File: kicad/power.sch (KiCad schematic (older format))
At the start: 30 parts, among them CON23 PS-ON, CON24 CON6, CON25 FAN, CON26 CON5x2, Q7 FDC6401N, Q8 FDC6401N, Q9 FDC6401N

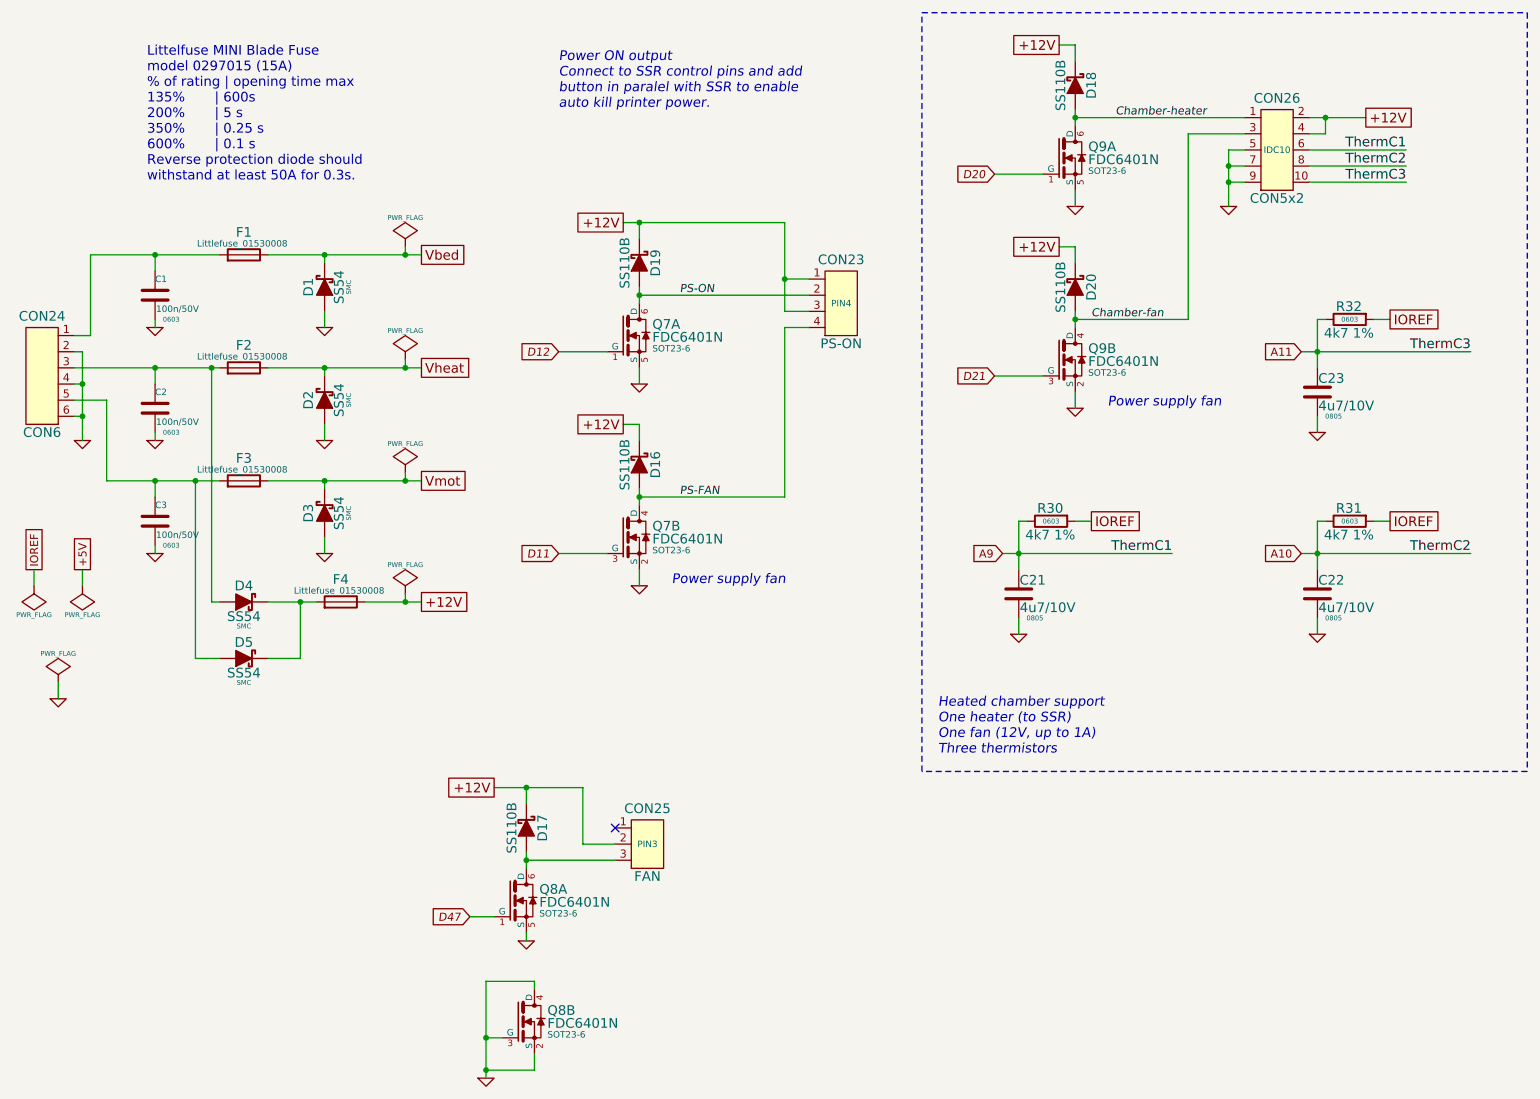
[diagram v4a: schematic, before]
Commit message: Add footprint informations
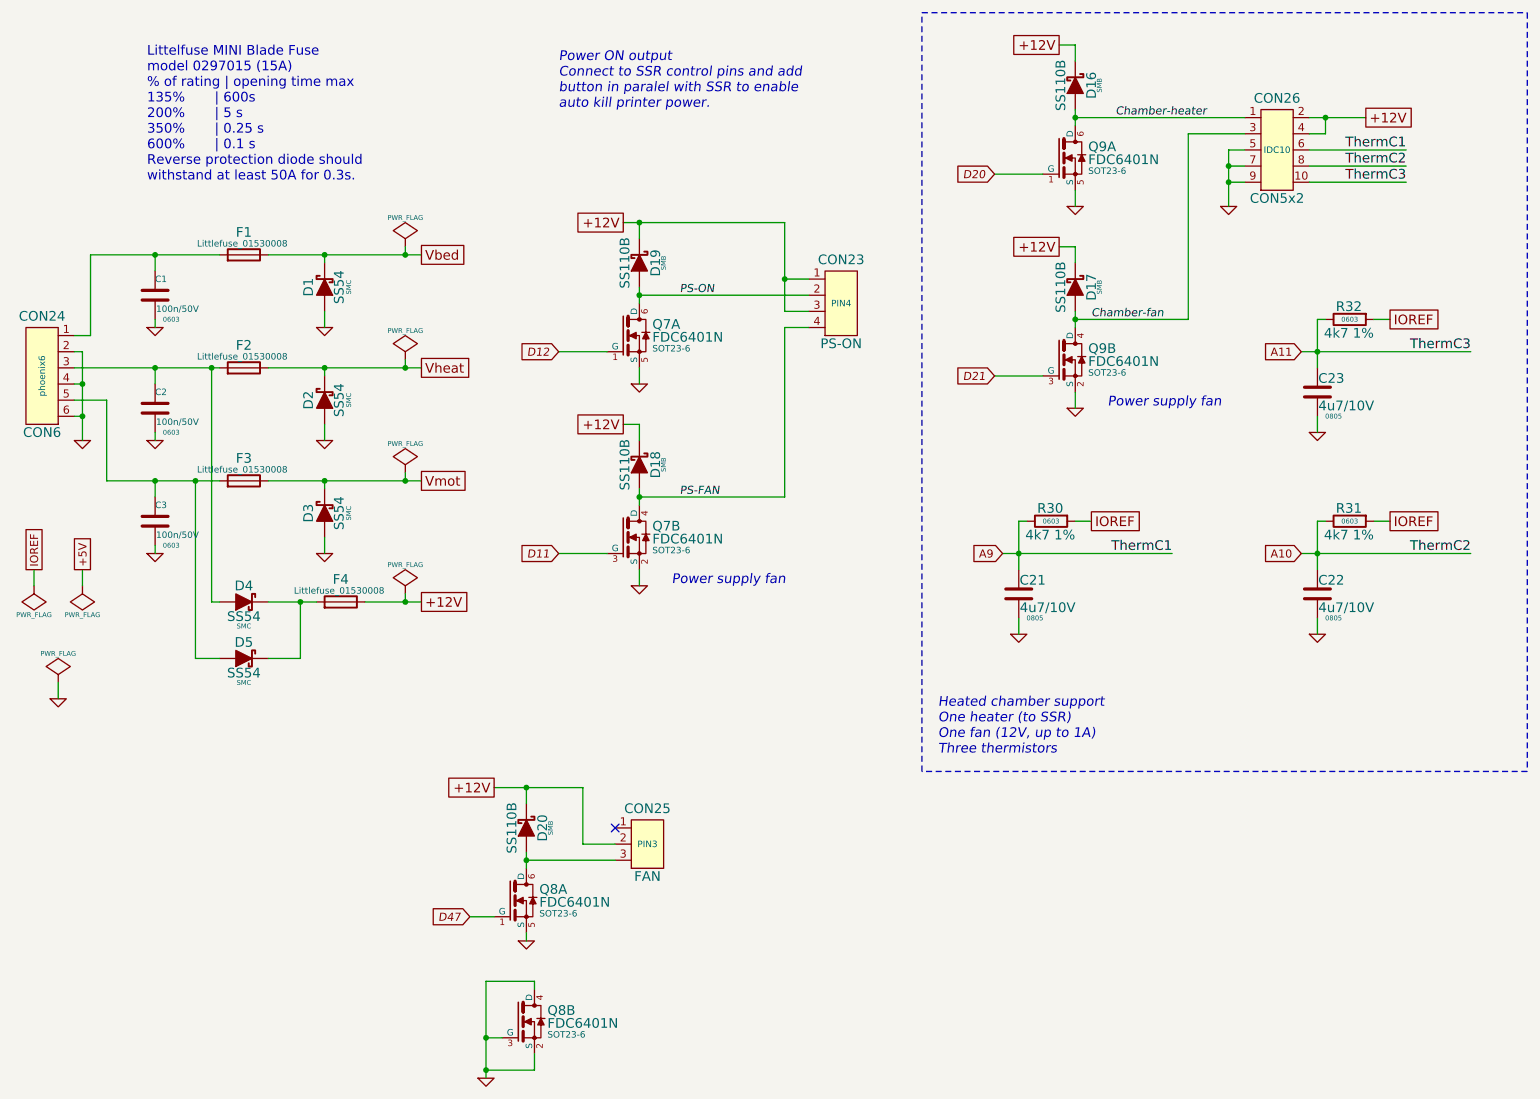
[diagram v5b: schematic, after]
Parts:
- CON24: footprint (none) -> phoenix6
- D16, D17, D18, D19, D20: footprint (none) -> SMB
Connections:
- net Chamber-fan: now also D17.2; no longer D20.2
- net Chamber-heater: now also D16.2; no longer D18.2
- net PS-FAN: now also D18.2; no longer D16.2
- net at CON25.3, Q8.6 (D): now also D20.2; no longer D17.2
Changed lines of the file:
@@
 $EndDescr
 $Comp
-L GND #PWR056
+L GND #PWR63
 U 1 1 53943822
 P 1400 3250
-F 0 "#PWR056" H 1400 3250 30  0001 C CNN
+F 0 "#PWR63" H 1400 3250 30  0001 C CNN
 F 1 "GND" H 1400 3180 30  0001 C CNN
 F 2 "" H 1400 3250 60  0000 C CNN
@@
 Littelfuse MINI Blade Fuse\nmodel 0297015 (15A)\n% of rating | opening time max\n135%       | 600s\n200%       | 5 s \n350%       | 0.25 s \n600%       | 0.1 s\nReverse protection diode should \nwithstand at least 50A for 0.3s.
 $Comp
-L GND #PWR057
+L GND #PWR65
 U 1 1 53943829
 P 2900 3250
-F 0 "#PWR057" H 2900 3250 30  0001 C CNN
+F 0 "#PWR65" H 2900 3250 30  0001 C CNN
 F 1 "GND" H 2900 3180 30  0001 C CNN
 F 2 "" H 2900 3250 60  0000 C CNN
@@
 $EndComp
 $Comp
-L GND #PWR058
+L GND #PWR59
 U 1 1 5394382F
 P 2900 2550
-F 0 "#PWR058" H 2900 2550 30  0001 C CNN
+F 0 "#PWR59" H 2900 2550 30  0001 C CNN
 F 1 "GND" H 2900 2480 30  0001 C CNN
 F 2 "" H 2900 2550 60  0000 C CNN
@@
 $EndComp
 $Comp
-L GND #PWR059
+L GND #PWR67
 U 1 1 53943835
 P 2900 3950
-F 0 "#PWR059" H 2900 3950 30  0001 C CNN
+F 0 "#PWR67" H 2900 3950 30  0001 C CNN
 F 1 "GND" H 2900 3880 30  0001 C CNN
 F 2 "" H 2900 3950 60  0000 C CNN
@@
 $EndComp
 $Comp
-L GND #PWR060
+L GND #PWR58
 U 1 1 53943842
 P 1850 2550
-F 0 "#PWR060" H 1850 2550 30  0001 C CNN
+F 0 "#PWR58" H 1850 2550 30  0001 C CNN
 F 1 "GND" H 1850 2480 30  0001 C CNN
 F 2 "" H 1850 2550 60  0000 C CNN
@@
 $EndComp
 $Comp
-L GND #PWR061
+L GND #PWR64
 U 1 1 53943848
 P 1850 3250
-F 0 "#PWR061" H 1850 3250 30  0001 C CNN
+F 0 "#PWR64" H 1850 3250 30  0001 C CNN
 F 1 "GND" H 1850 3180 30  0001 C CNN
 F 2 "" H 1850 3250 60  0000 C CNN
@@
 $EndComp
 $Comp
-L GND #PWR062
+L GND #PWR66
 U 1 1 5394384E
 P 1850 3950
-F 0 "#PWR062" H 1850 3950 30  0001 C CNN
+F 0 "#PWR66" H 1850 3950 30  0001 C CNN
 F 1 "GND" H 1850 3880 30  0001 C CNN
 F 2 "" H 1850 3950 60  0000 C CNN
@@
 F 0 "CON24" H 1150 3220 60  0000 C CNN
 F 1 "CON6" H 1150 2500 60  0000 C CNN
-F 2 "" H 1150 2850 40  0000 C CNN
+F 2 "phoenix6" V 1150 2850 40  0000 C CNN
 F 3 "" H 1150 2850 40  0000 C CNN
 	1    1150 2850
@@
 $EndComp
 $Comp
-L PWR_FLAG #FLG063
+L PWR_FLAG #FLG1
 U 1 1 539438AC
 P 3400 2050
-F 0 "#FLG063" H 3400 2145 30  0001 C CNN
+F 0 "#FLG1" H 3400 2145 30  0001 C CNN
 F 1 "PWR_FLAG" H 3400 2230 30  0000 C CNN
 F 2 "" H 3400 2050 60  0000 C CNN
@@
 $EndComp
 $Comp
-L PWR_FLAG #FLG064
+L PWR_FLAG #FLG2
 U 1 1 539438B2
 P 3400 2750
-F 0 "#FLG064" H 3400 2845 30  0001 C CNN
+F 0 "#FLG2" H 3400 2845 30  0001 C CNN
 F 1 "PWR_FLAG" H 3400 2930 30  0000 C CNN
 F 2 "" H 3400 2750 60  0000 C CNN
@@
 $EndComp
 $Comp
-L PWR_FLAG #FLG065
+L PWR_FLAG #FLG3
 U 1 1 539438B8
 P 3400 3450
-F 0 "#FLG065" H 3400 3545 30  0001 C CNN
+F 0 "#FLG3" H 3400 3545 30  0001 C CNN
 F 1 "PWR_FLAG" H 3400 3630 30  0000 C CNN
 F 2 "" H 3400 3450 60  0000 C CNN
@@
 $EndComp
 $Comp
-L PWR_FLAG #FLG066
+L PWR_FLAG #FLG6
 U 1 1 539438BE
 P 3400 4200
-F 0 "#FLG066" H 3400 4295 30  0001 C CNN
+F 0 "#FLG6" H 3400 4295 30  0001 C CNN
 F 1 "PWR_FLAG" H 3400 4380 30  0000 C CNN
 F 2 "" H 3400 4200 60  0000 C CNN
@@
 $EndComp
 $Comp
-L PWR_FLAG #FLG067
+L PWR_FLAG #FLG7
 U 1 1 539438C4
 P 1250 4750
-F 0 "#FLG067" H 1250 4845 30  0001 C CNN
+F 0 "#FLG7" H 1250 4845 30  0001 C CNN
 F 1 "PWR_FLAG" H 1250 4930 30  0000 C CNN
 F 2 "" H 1250 4750 60  0000 C CNN
@@
 $EndComp
 $Comp
-L GND #PWR068
+L GND #PWR71
 U 1 1 539438CA
 P 1250 4850
-F 0 "#PWR068" H 1250 4850 30  0001 C CNN
+F 0 "#PWR71" H 1250 4850 30  0001 C CNN
 F 1 "GND" H 1250 4780 30  0001 C CNN
 F 2 "" H 1250 4850 60  0000 C CNN
@@
 IOREF
 $Comp
-L PWR_FLAG #FLG069
+L PWR_FLAG #FLG5
 U 1 1 53943908
 P 1400 4150
-F 0 "#FLG069" H 1400 4245 30  0001 C CNN
+F 0 "#FLG5" H 1400 4245 30  0001 C CNN
 F 1 "PWR_FLAG" H 1400 4330 30  0000 C CNN
 F 2 "" H 1400 4150 60  0000 C CNN
@@
 $EndComp
 $Comp
-L PWR_FLAG #FLG070
+L PWR_FLAG #FLG4
 U 1 1 5394390F
 P 1100 4150
-F 0 "#FLG070" H 1100 4245 30  0001 C CNN
+F 0 "#FLG4" H 1100 4245 30  0001 C CNN
 F 1 "PWR_FLAG" H 1100 4330 30  0000 C CNN
 F 2 "" H 1100 4150 60  0000 C CNN
@@
 $EndComp
 $Comp
-L GND #PWR071
+L GND #PWR68
 U 1 1 53943ED6
 P 4850 4150
-F 0 "#PWR071" H 4850 4150 30  0001 C CNN
+F 0 "#PWR68" H 4850 4150 30  0001 C CNN
 F 1 "GND" H 4850 4080 30  0001 C CNN
 F 2 "" H 4850 4150 60  0000 C CNN
@@
 $EndComp
 $Comp
-L GND #PWR072
+L GND #PWR60
 U 1 1 53943F43
 P 4850 2900
-F 0 "#PWR072" H 4850 2900 30  0001 C CNN
+F 0 "#PWR60" H 4850 2900 30  0001 C CNN
 F 1 "GND" H 4850 2830 30  0001 C CNN
 F 2 "" H 4850 2900 60  0000 C CNN
@@
 	5750 1900 5750 2450
 Connection ~ 5750 2250
-$Comp
-L SS110B D16
-U 1 1 53948052
-P 4850 3400
-F 0 "D16" H 4850 3300 60  0000 C CNN
-F 1 "SS110B" H 4850 3490 60  0000 C CNN
-F 2 "" V 4700 3362 30  0000 C CNN
-F 3 "" V 4850 3400 60  0000 C CNN
-	1    4850 3400
-	0    -1   -1   0
-$EndComp
 Wire Wire Line
 	4850 3250 4850 3150
@@
 	1    0    0    -1
 $EndComp
-$Comp
-L SS110B D17
-U 1 1 539489C2
-P 4150 5650
-F 0 "D17" H 4150 5550 60  0000 C CNN
-F 1 "SS110B" H 4150 5740 60  0000 C CNN
-F 2 "" V 4000 5612 30  0000 C CNN
-F 3 "" V 4150 5650 60  0000 C CNN
-	1    4150 5650
-	0    -1   -1   0
-$EndComp
 Wire Wire Line
 	4150 5800 4150 5900
@@
 D47
 $Comp
-L GND #PWR073
+L GND #PWR72
 U 1 1 53948CCE
 P 4150 6350
-F 0 "#PWR073" H 4150 6350 30  0001 C CNN
+F 0 "#PWR72" H 4150 6350 30  0001 C CNN
 F 1 "GND" H 4150 6280 30  0001 C CNN
 F 2 "" H 4150 6350 60  0000 C CNN
@@
 Connection ~ 3900 7150
 $Comp
-L GND #PWR074
+L GND #PWR73
 U 1 1 53949810
 P 3900 7200
-F 0 "#PWR074" H 3900 7200 30  0001 C CNN
+F 0 "#PWR73" H 3900 7200 30  0001 C CNN
 F 1 "GND" H 3900 7130 30  0001 C CNN
 F 2 "" H 3900 7200 60  0000 C CNN
@@
 F 0 "D19" H 4850 2050 60  0000 C CNN
 F 1 "SS110B" H 4850 2240 60  0000 C CNN
-F 2 "" V 4700 2112 30  0000 C CNN
+F 2 "SMB" H 4850 2000 30  0000 C CNN
 F 3 "" V 4850 2150 60  0000 C CNN
 	1    4850 2150
@@
 $EndComp
 $Comp
-L GND #PWR075
+L GND #PWR61
 U 1 1 5394A1DE
 P 7550 3050
-F 0 "#PWR075" H 7550 3050 30  0001 C CNN
+F 0 "#PWR61" H 7550 3050 30  0001 C CNN
 F 1 "GND" H 7550 2980 30  0001 C CNN
 F 2 "" H 7550 3050 60  0000 C CNN
@@
 $EndComp
 $Comp
-L GND #PWR076
+L GND #PWR56
 U 1 1 5394A1E4
 P 7550 1800
-F 0 "#PWR076" H 7550 1800 30  0001 C CNN
+F 0 "#PWR56" H 7550 1800 30  0001 C CNN
 F 1 "GND" H 7550 1730 30  0001 C CNN
 F 2 "" H 7550 1800 60  0000 C CNN
@@
 Wire Wire Line
 	7550 2950 7550 3050
-$Comp
-L SS110B D20
-U 1 1 5394A1F7
-P 7550 2300
-F 0 "D20" H 7550 2200 60  0000 C CNN
-F 1 "SS110B" H 7550 2390 60  0000 C CNN
-F 2 "" V 7400 2262 30  0000 C CNN
-F 3 "" V 7550 2300 60  0000 C CNN
-	1    7550 2300
-	0    -1   -1   0
-$EndComp
 Wire Wire Line
 	7550 2150 7550 2050
@@
 Text Label 7650 2500 0    50   Italic 0
 Chamber-fan
-$Comp
-L SS110B D18
-U 1 1 5394A209
-P 7550 1050
-F 0 "D18" H 7550 950 60  0000 C CNN
-F 1 "SS110B" H 7550 1140 60  0000 C CNN
-F 2 "" V 7400 1012 30  0000 C CNN
-F 3 "" V 7550 1050 60  0000 C CNN
-	1    7550 1050
-	0    -1   -1   0
-$EndComp
 Wire Wire Line
 	7550 900  7550 800
@@
 Connection ~ 8500 1550
 $Comp
-L GND #PWR077
+L GND #PWR57
 U 1 1 5394B08E
 P 8500 1800
-F 0 "#PWR077" H 8500 1800 30  0001 C CNN
+F 0 "#PWR57" H 8500 1800 30  0001 C CNN
 F 1 "GND" H 8500 1730 30  0001 C CNN
 F 2 "" H 8500 1800 60  0000 C CNN
@@
 $EndComp
 $Comp
-L GND #PWR078
+L GND #PWR69
 U 1 1 5394B617
 P 7200 4450
-F 0 "#PWR078" H 7200 4450 30  0001 C CNN
+F 0 "#PWR69" H 7200 4450 30  0001 C CNN
 F 1 "GND" H 7200 4380 30  0001 C CNN
 F 2 "~" H 7200 4450 60  0000 C CNN
@@
 $EndComp
 $Comp
-L GND #PWR079
+L GND #PWR70
 U 1 1 5394B93D
 P 9050 4450
-F 0 "#PWR079" H 9050 4450 30  0001 C CNN
+F 0 "#PWR70" H 9050 4450 30  0001 C CNN
 F 1 "GND" H 9050 4380 30  0001 C CNN
 F 2 "~" H 9050 4450 60  0000 C CNN
@@
 $EndComp
 $Comp
-L GND #PWR080
+L GND #PWR62
 U 1 1 5394BA08
 P 9050 3200
-F 0 "#PWR080" H 9050 3200 30  0001 C CNN
+F 0 "#PWR62" H 9050 3200 30  0001 C CNN
 F 1 "GND" H 9050 3130 30  0001 C CNN
 F 2 "~" H 9050 3200 60  0000 C CNN
@@
 Text Notes 6700 5200 0    60   Italic 0
 Heated chamber support\nOne heater (to SSR)\nOne fan (12V, up to 1A)\nThree thermistors
+$Comp
+L SS110B D18
+U 1 1 539B1F63
+P 4850 3400
+F 0 "D18" H 4850 3300 60  0000 C CNN
+F 1 "SS110B" H 4850 3490 60  0000 C CNN
+F 2 "SMB" H 4850 3250 30  0000 C CNN
+F 3 "" V 4850 3400 60  0000 C CNN
+	1    4850 3400
+	0    -1   -1   0
+$EndComp
+$Comp
+L SS110B D17
+U 1 1 539B1FBA
+P 7550 2300
+F 0 "D17" H 7550 2200 60  0000 C CNN
+F 1 "SS110B" H 7550 2390 60  0000 C CNN
+F 2 "SMB" H 7550 2150 30  0000 C CNN
+F 3 "" V 7550 2300 60  0000 C CNN
+	1    7550 2300
+	0    -1   -1   0
+$EndComp
+$Comp
+L SS110B D16
+U 1 1 539B202A
+P 7550 1050
+F 0 "D16" H 7550 950 60  0000 C CNN
+F 1 "SS110B" H 7550 1140 60  0000 C CNN
+F 2 "SMB" H 7550 900 30  0000 C CNN
+F 3 "" V 7550 1050 60  0000 C CNN
+	1    7550 1050
+	0    -1   -1   0
+$EndComp
+$Comp
+L SS110B D20
+U 1 1 539B228F
+P 4150 5650
+F 0 "D20" H 4150 5550 60  0000 C CNN
+F 1 "SS110B" H 4150 5740 60  0000 C CNN
+F 2 "SMB" H 4150 5500 30  0000 C CNN
+F 3 "" V 4150 5650 60  0000 C CNN
+	1    4150 5650
+	0    -1   -1   0
+$EndComp
 $EndSCHEMATC
